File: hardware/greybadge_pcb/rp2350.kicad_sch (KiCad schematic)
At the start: 38 parts, among them J6 SM03B-SRSS-TB, J7 USB_C_Receptacle_USB2.0, SW2 SW_Push, SW3 SW_Push, U6 W25Q128JVS, U7 RP2350_60QFN, U8 NCP1117-3.3_SOT223, Y1 12Mhz

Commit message: feat: rough component placement
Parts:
- added C1: 10u, Capacitor_SMD:C_0805_2012Metric, symbol Device:C
- added GC9A1: CG9A01, footprints:GC9A01, symbol maimai:CG9A01
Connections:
- net +3V3: now also C1.1, GC9A1.7 (VCC)
- net GND: now also C1.2, GC9A1.6 (GND)
- net GPIO2 renamed OLED_SCL
- net OLED_SCL: now also GC9A1.5 (SCL)
- net GPIO3 renamed OLED_SDA
- net OLED_SDA: now also GC9A1.4 (SDA)
- net GPIO4 renamed OLED_DC
- net OLED_DC: now also GC9A1.3 (DC)
- net GPIO5 renamed OLED_CS
- net OLED_CS: now also GC9A1.2 (CS)
- net GPIO6 renamed OLED_RST
- net OLED_RST: now also GC9A1.1 (RST)
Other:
- note added: "Display"

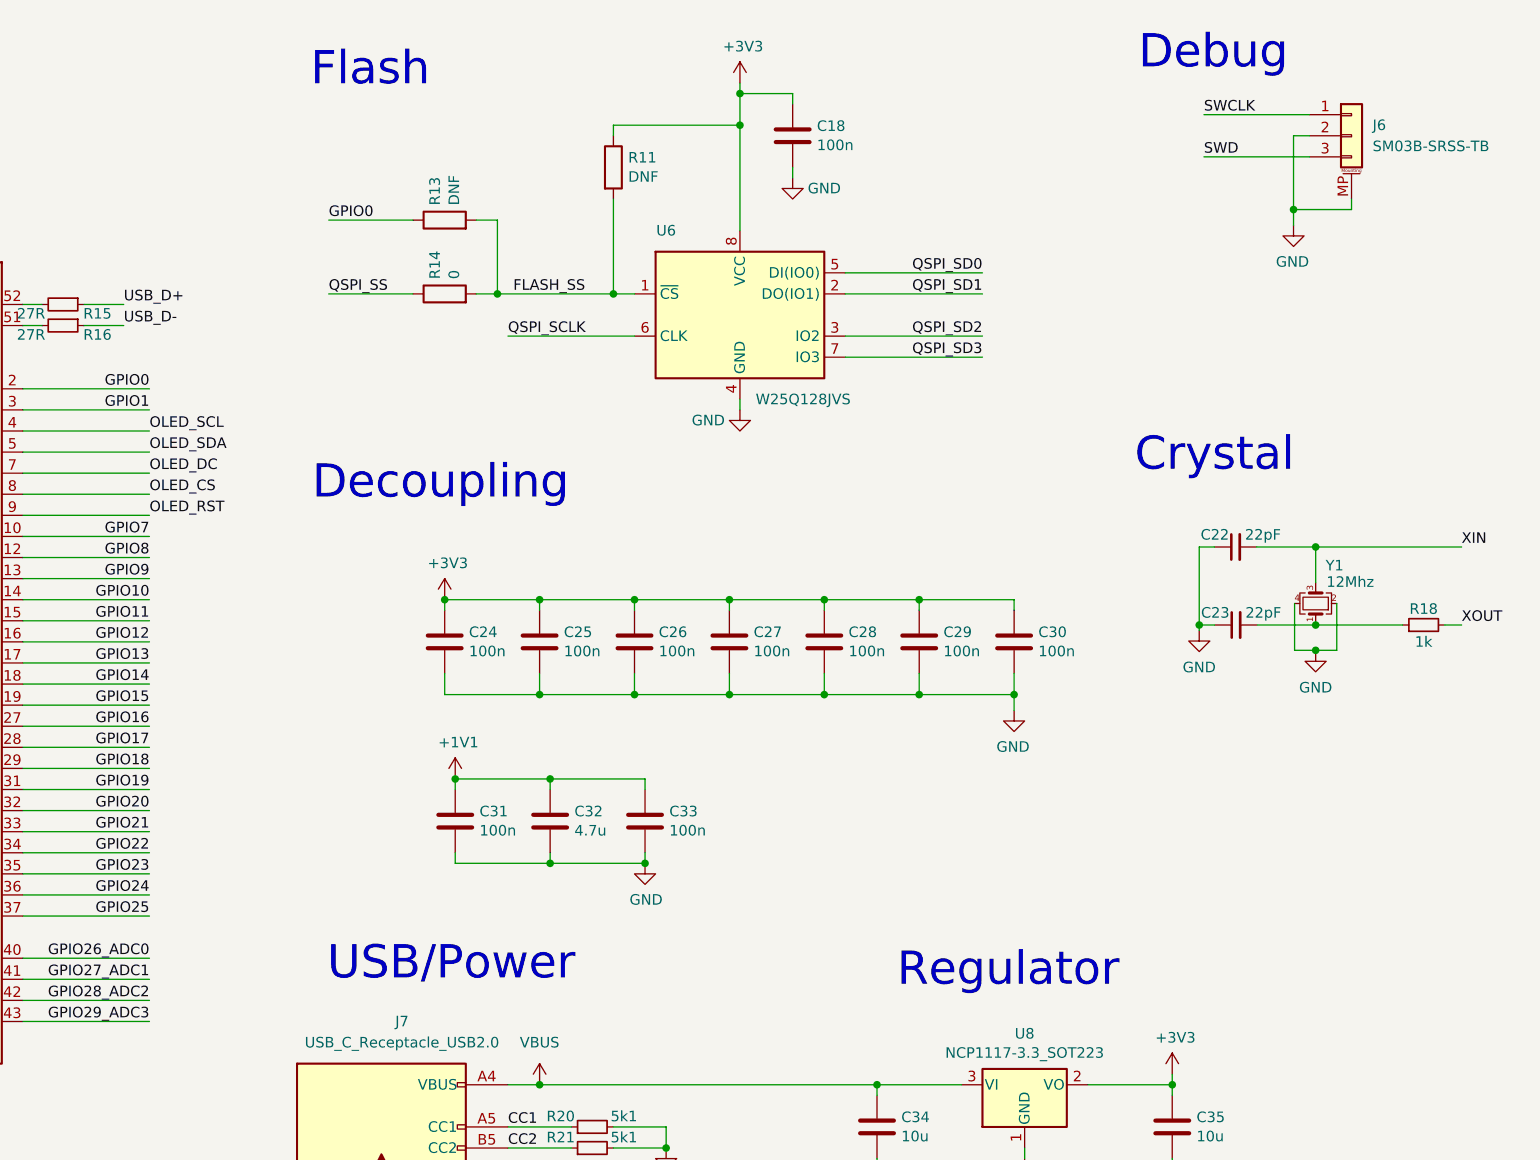
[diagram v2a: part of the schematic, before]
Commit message: feat: bga and mcu routing
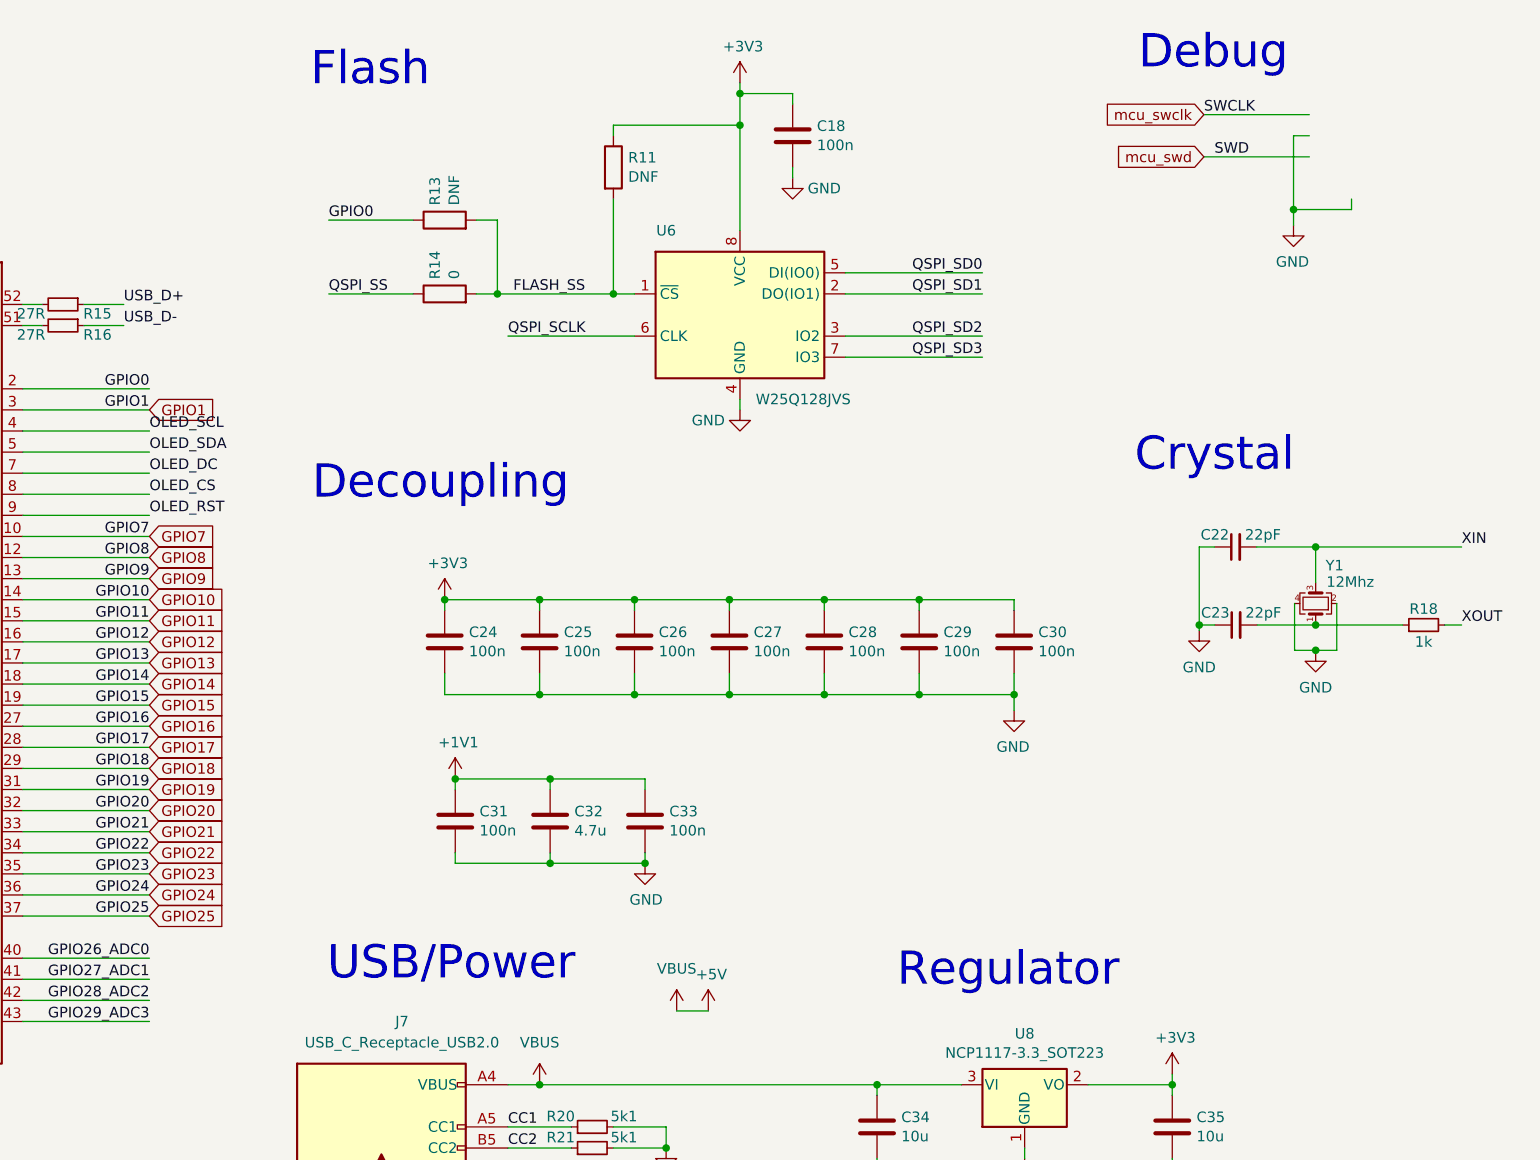
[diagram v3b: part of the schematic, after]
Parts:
- removed J6: SM03B-SRSS-TB, Connector_JST:JST_SH_SM03B-SRSS-TB_1x03-1MP_P1.00mm_Horizontal, symbol Connector_Generic_MountingPin:Conn_01x03_MountingPin
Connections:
- net SWCLK renamed mcu_swclk
- net SWD renamed mcu_swd
- net VBUS renamed +5V

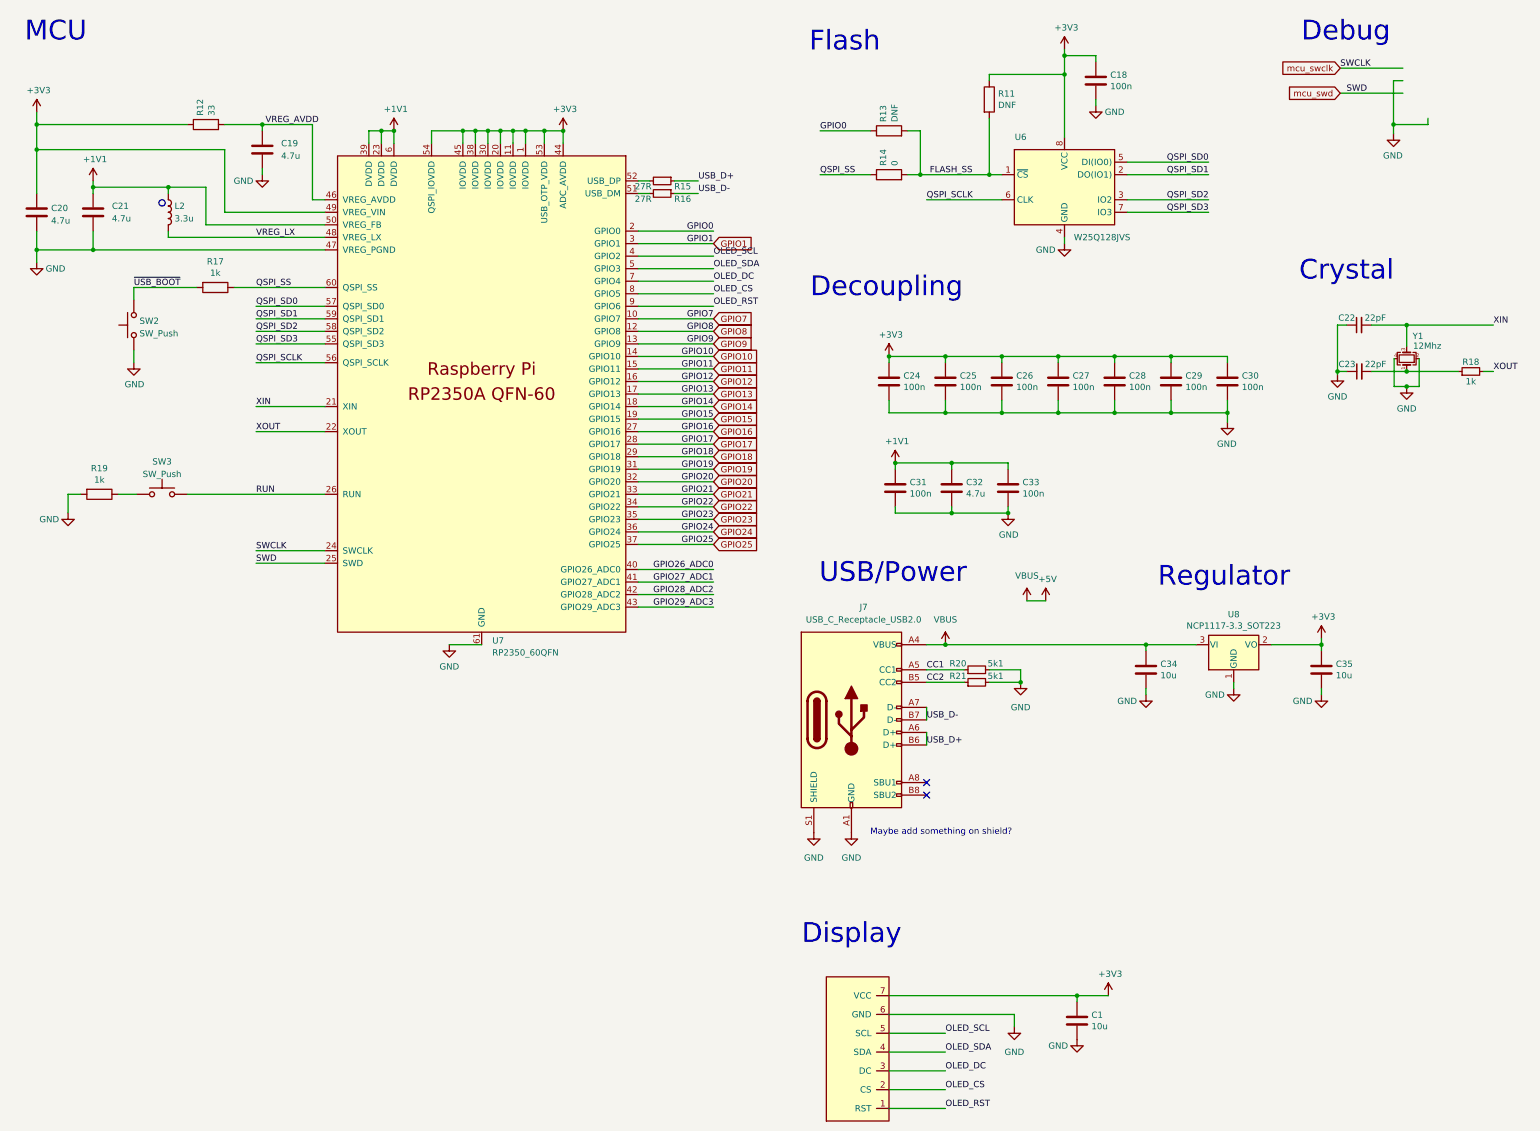
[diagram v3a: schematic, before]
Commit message: Fix annotation
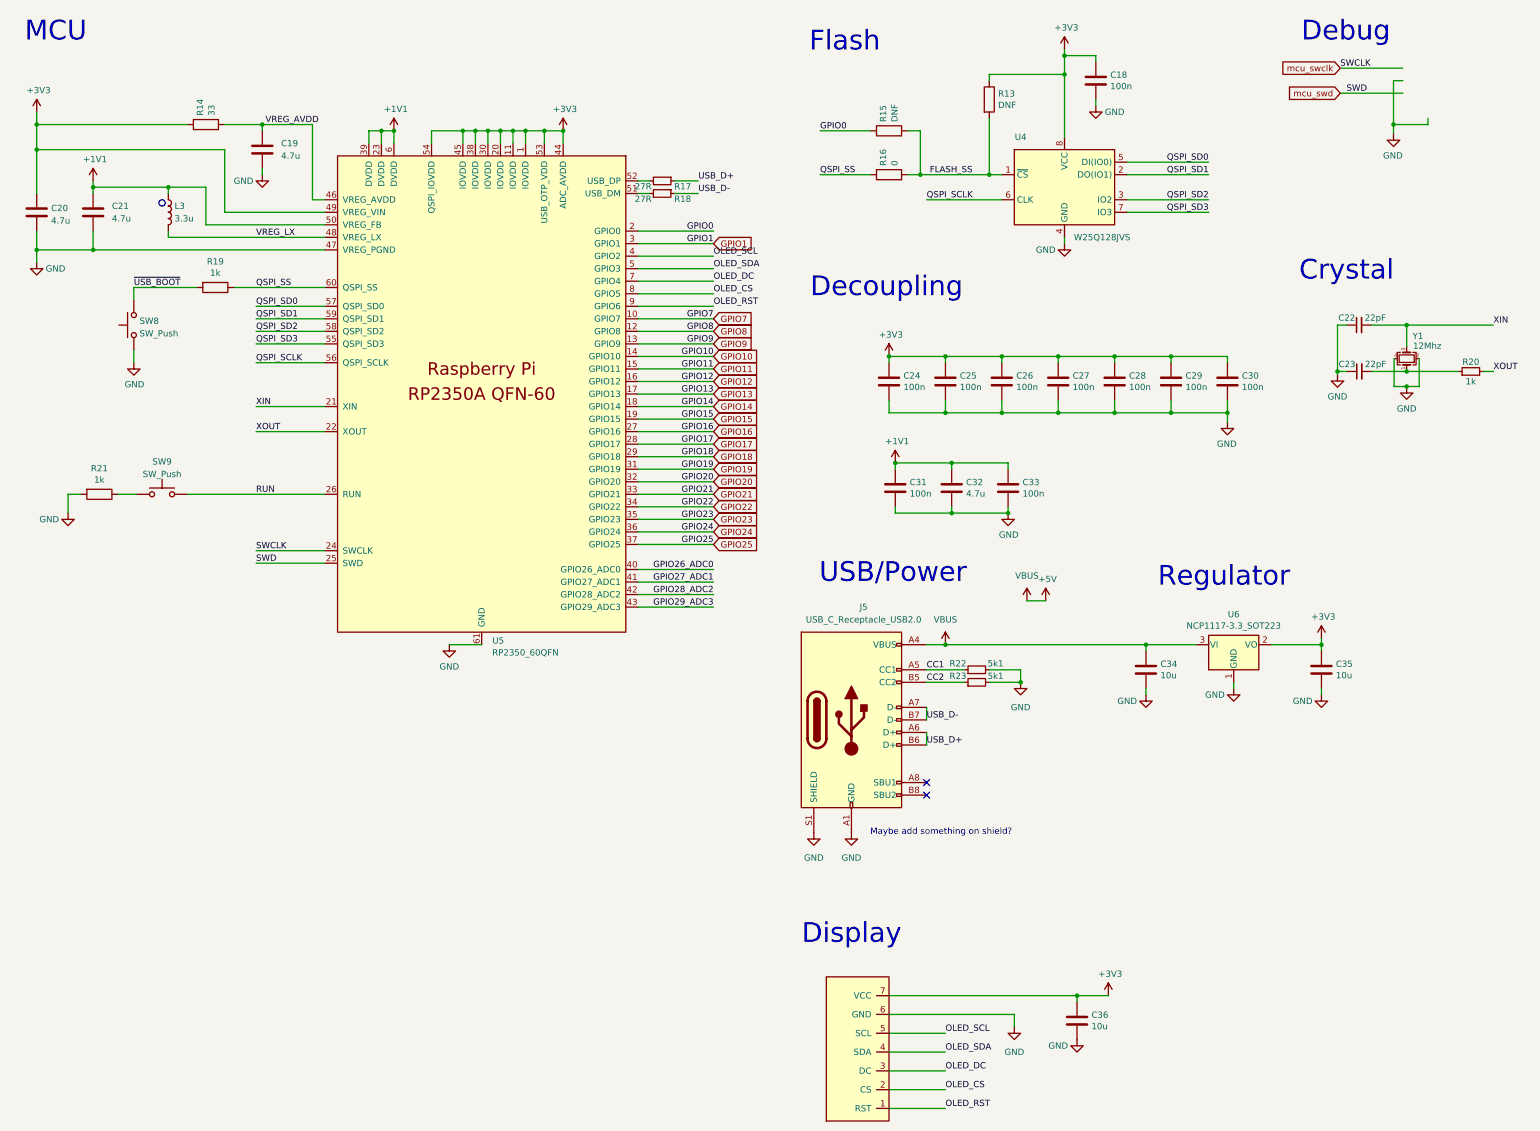
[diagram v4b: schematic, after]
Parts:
- renumbered C1 to C36, J7 to J5, L2 to L3, R11 to R13, R12 to R14, R13 to R15, R14 to R16, R15 to R17, R16 to R18, R17 to R19, R18 to R20, R19 to R21, R20 to R22, R21 to R23, SW2 to SW8, SW3 to SW9, U6 to U4, U7 to U5, U8 to U6

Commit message: feat: leds
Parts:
- removed SW8, SW9: SW_Push, Button_Switch_SMD:SW_Push_1P1T_NO_Vertical_Wuerth_434133025816, symbol Switch:SW_Push
- added SW? (x2): SW_Push, Button_Switch_SMD:SW_Push_1P1T_XKB_TS-1187A, symbol Switch:SW_Push
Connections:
- net GND: now also SW?.2
- net RUN: now also SW?.1
- net ~{USB_BOOT}: now also SW?.1
- net at R21.1: now also SW?.2
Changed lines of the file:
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@@
 	(wire
 		(pts
-			(xy 45.085 86.36) (xy 45.085 88.9)
-		)
-		(stroke
-			(width 0)
-			(type default)
-		)
-	)
-	(wire
-		(pts
 			(xy 250.19 154.94) (xy 250.19 156.21)
 		)
@@
 	(wire
 		(pts
+			(xy 44.45 86.36) (xy 44.45 88.9)
+		)
+		(stroke
+			(width 0)
+			(type default)
+		)
+	)
+	(wire
+		(pts
 			(xy 199.39 109.22) (xy 210.82 109.22)
 		)
@@
 	(wire
 		(pts
-			(xy 45.085 73.66) (xy 45.085 76.2)
+			(xy 44.45 73.66) (xy 44.45 76.2)
 		)
 		(stroke
@@
 	(wire
 		(pts
-			(xy 57.785 73.66) (xy 45.085 73.66)
+			(xy 57.785 73.66) (xy 44.45 73.66)
 		)
 		(stroke
@@
 	(symbol
 		(lib_id "power:GND")
-		(at 45.085 88.9 0)
+		(at 44.45 88.9 0)
 		(unit 1)
 		(exclude_from_sim no)
@@
 		(dnp no)
 		(property "Reference" "#PWR069"
-			(at 45.085 95.25 0)
+			(at 44.45 95.25 0)
 			(effects
 				(font
@@
 		)
 		(property "Value" "GND"
-			(at 45.212 93.2942 0)
+			(at 44.577 93.2942 0)
 			(effects
 				(font
@@
 		)
 		(property "Footprint" ""
-			(at 45.085 88.9 0)
+			(at 44.45 88.9 0)
 			(effects
 				(font
@@
 		)
 		(property "Datasheet" ""
-			(at 45.085 88.9 0)
+			(at 44.45 88.9 0)
 			(effects
 				(font
@@
 		)
 		(property "Description" ""
-			(at 45.085 88.9 0)
+			(at 44.45 88.9 0)
 			(effects
 				(font
@@
 	)
 	(symbol
+		(lib_id "Switch:SW_Push")
+		(at 50.8 115.57 0)
+		(mirror y)
+		(unit 1)
+		(exclude_from_sim no)
+		(in_bom yes)
+		(on_board yes)
+		(dnp no)
+		(property "Reference" "SW?"
+			(at 50.8 107.95 0)
+			(effects
+				(font
+					(size 1.27 1.27)
+				)
+			)
+		)
+		(property "Value" "SW_Push"
+			(at 50.8 110.49 0)
+			(effects
+				(font
+					(size 1.27 1.27)
+				)
+			)
+		)
+		(property "Footprint" "Button_Switch_SMD:SW_Push_1P1T_XKB_TS-1187A"
+			(at 50.8 110.49 0)
+			(effects
+				(font
+					(size 1.27 1.27)
+				)
+				(hide yes)
+			)
+		)
+		(property "Datasheet" "~"
+			(at 50.8 110.49 0)
+			(effects
+				(font
+					(size 1.27 1.27)
+				)
+				(hide yes)
+			)
+		)
+		(property "Description" "Push button switch, generic, two pins"
+			(at 50.8 115.57 0)
+			(effects
+				(font
+					(size 1.27 1.27)
+				)
+				(hide yes)
+			)
+		)
+		(pin "2"
+		)
+		(pin "1"
+		)
+		(instances
+			(project "greybadge_pcb"
+				(path "/4eb7ff30-5b75-4e83-8e37-4e6cd7a9e830/9563b0f2-de2f-44b6-a21c-14dec17cccec"
+					(reference "SW?")
+					(unit 1)
+				)
+			)
+		)
+	)
+	(symbol
 		(lib_id "Device:C")
 		(at 240.03 31.75 0)
@@
 	)
 	(symbol
-		(lib_id "Switch:SW_Push")
-		(at 45.085 81.28 90)
-		(unit 1)
-		(exclude_from_sim no)
-		(in_bom yes)
-		(on_board yes)
-		(dnp no)
-		(fields_autoplaced yes)
-		(property "Reference" "SW8"
-			(at 46.228 80.4453 90)
-			(effects
-				(font
-					(size 1.27 1.27)
-				)
-				(justify right)
-			)
-		)
-		(property "Value" "SW_Push"
-			(at 46.228 82.9822 90)
-			(effects
-				(font
-					(size 1.27 1.27)
-				)
-				(justify right)
-			)
-		)
-		(property "Footprint" "Button_Switch_SMD:SW_Push_1P1T_NO_Vertical_Wuerth_434133025816"
-			(at 40.005 81.28 0)
-			(effects
-				(font
-					(size 1.27 1.27)
-				)
-				(hide yes)
-			)
-		)
-		(property "Datasheet" "~"
-			(at 40.005 81.28 0)
-			(effects
-				(font
-					(size 1.27 1.27)
-				)
-				(hide yes)
-			)
-		)
-		(property "Description" ""
-			(at 45.085 81.28 0)
-			(effects
-				(font
-					(size 1.27 1.27)
-				)
-			)
-		)
-		(pin "1"
-		)
-		(pin "2"
-		)
-		(instances
-			(project "greybadge_pcb"
-				(path "/4eb7ff30-5b75-4e83-8e37-4e6cd7a9e830/9563b0f2-de2f-44b6-a21c-14dec17cccec"
-					(reference "SW8")
-					(unit 1)
-				)
-			)
-		)
-	)
-	(symbol
 		(lib_id "Memory_Flash:W25Q128JVS")
 		(at 233.68 53.34 0)
@@
 	)
 	(symbol
-		(lib_id "Switch:SW_Push")
-		(at 50.8 115.57 0)
-		(unit 1)
-		(exclude_from_sim no)
-		(in_bom yes)
-		(on_board yes)
-		(dnp no)
-		(fields_autoplaced yes)
-		(property "Reference" "SW9"
-			(at 50.8 108.9492 0)
-			(effects
-				(font
-					(size 1.27 1.27)
-				)
-			)
-		)
-		(property "Value" "SW_Push"
-			(at 50.8 111.4861 0)
-			(effects
-				(font
-					(size 1.27 1.27)
-				)
-			)
-		)
-		(property "Footprint" "Button_Switch_SMD:SW_Push_1P1T_NO_Vertical_Wuerth_434133025816"
-			(at 50.8 110.49 0)
-			(effects
-				(font
-					(size 1.27 1.27)
-				)
-				(hide yes)
-			)
-		)
-		(property "Datasheet" "~"
-			(at 50.8 110.49 0)
-			(effects
-				(font
-					(size 1.27 1.27)
-				)
-				(hide yes)
-			)
-		)
-		(property "Description" ""
-			(at 50.8 115.57 0)
-			(effects
-				(font
-					(size 1.27 1.27)
-				)
-			)
-		)
-		(pin "1"
-		)
-		(pin "2"
-		)
-		(instances
-			(project "greybadge_pcb"
-				(path "/4eb7ff30-5b75-4e83-8e37-4e6cd7a9e830/9563b0f2-de2f-44b6-a21c-14dec17cccec"
-					(reference "SW9")
-					(unit 1)
-				)
-			)
-		)
-	)
-	(symbol
 		(lib_id "power:GND")
 		(at 222.25 119.38 0)
@@
 					(unit 1)
 				)
+			)
+		)
+	)
+	(symbol
+		(lib_id "Switch:SW_Push")
+		(at 44.45 81.28 90)
+		(mirror x)
+		(unit 1)
+		(exclude_from_sim no)
+		(in_bom yes)
+		(on_board yes)
+		(dnp no)
+		(property "Reference" "SW?"
+			(at 36.83 81.28 0)
+			(effects
+				(font
+					(size 1.27 1.27)
+				)
+			)
+		)
+		(property "Value" "SW_Push"
+			(at 39.37 81.28 0)
+			(effects
+				(font
+					(size 1.27 1.27)
+				)
+			)
+		)
+		(property "Footprint" "Button_Switch_SMD:SW_Push_1P1T_XKB_TS-1187A"
+			(at 39.37 81.28 0)
+			(effects
+				(font
+					(size 1.27 1.27)
+				)
+				(hide yes)
+			)
+		)
+		(property "Datasheet" "~"
+			(at 39.37 81.28 0)
+			(effects
+				(font
+					(size 1.27 1.27)
+				)
+				(hide yes)
+			)
+		)
+		(property "Description" "Push button switch, generic, two pins"
+			(at 44.45 81.28 0)
+			(effects
+				(font
+					(size 1.27 1.27)
+				)
+				(hide yes)
+			)
+		)
+		(pin "2"
+		)
+		(pin "1"
+		)
+		(instances
+			(project "greybadge_pcb"
+				(path "/4eb7ff30-5b75-4e83-8e37-4e6cd7a9e830/9563b0f2-de2f-44b6-a21c-14dec17cccec"
+					(reference "SW?")
+					(unit 1)
+				)
